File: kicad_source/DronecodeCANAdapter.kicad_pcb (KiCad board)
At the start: 2 copper layers, 65 x 30 mm, 31 parts, among them CN1 RASPI-IO, CN2 691322310004, CN3 GH_SM04B-GHS-TB, CN4 GH_SM04B-GHS-TB, SW1 JS202011JCQN, U1 MCP2518FD, U2 TCAN332GDR, Y1 RH100-20.000-20-3030-TR

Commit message: updated schematic and layout
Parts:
- removed C2, C3: 22pF, capacitors:C_0603
- removed C4: 100nF, capacitors:C_0603
- removed the D3 at (127.5, 94.5)
- removed L2: Label, labels:generationmake_logo
- removed R10, R11: 1k, resistors:R_0603
- removed R12: 2k, resistors:R_0603
- removed R5: 10k, resistors:R_0603
- removed R6, R7, R9: DNI, resistors:R_0603
- removed R8: 0R, resistors:R_0603
- removed SW1: JS202011JCQN, mechanical-switches:CK_JS202011JCQN
- removed U2: TCAN332GDR, SOIC:SOIJ-8_5.3x5.3mm_Pitch1.27mm
- removed Y1: RH100-20.000-20-3030-TR, crystals:Crystal_SMD_3.2x2.5mm_4Pad
- added D1: 150060GS75000, LEDs:LED_0603, F.Cu at (140.5, 98.0)
- added MECH1: MHP_3.2_5.0, MECH_mounting_holes:MHP_3.2_5.0, F.Cu at (140.5, 102.0)
- added MECH2: MHP_3.2_5.0, MECH_mounting_holes:MHP_3.2_5.0, F.Cu at (155.5, 102.0)
- CN1: value RASPI-IO -> CONN_01X05; footprint MODULE_compute:RASPI_ZERO_HAT_EDGE -> pin_headers:Pin_Header_Straight_1x05
- CN2: moved to B.Cu
- D2: value 150060GS75000 -> 150060RS75000
- L1: footprint labels:generationmake_small_solder -> labels:generationmake_small_silk; moved to B.Cu
- R1: value 0R -> 1k
- R2: value DNI -> 1k
- R3: value 10k -> 2k
- R4: value 120R -> DNI
- U1: value MCP2518FD -> TCAN332GDR; footprint SOIC:SOIC-14_3.9x8.7mm_Pitch1.27mm -> SOIC:SOIJ-8_5.3x5.3mm_Pitch1.27mm
- moved R4 27.4 mm to (144.0, 105.0), turned to 270 degrees
- moved C1 24.9 mm to (148.0, 96.5)
- moved CN2 24.5 mm to (148.0, 108.5), turned to 180 degrees
- moved D2 24.3 mm to (155.5, 98.0), turned to 180 degrees
- moved L1 22.7 mm to (148.0, 100.8), turned to 180 degrees
- moved R3 18.4 mm to (156.9, 109.0), turned to 90 degrees
- moved U1 10.4 mm to (148.0, 102.0), turned to 270 degrees
- moved D3 8.03 mm to (156.9, 106.2), turned to 270 degrees
- moved F1 7.68 mm to (141.4, 106.2), turned to 180 degrees
- moved CN1 4.61 mm to (143.0, 93.5), turned to 90 degrees
- moved R2 3.64 mm to (152.5, 98.0), turned to 0 degrees
- moved R1 2.69 mm to (143.5, 98.0), turned to 180 degrees
- moved D4 0.73 mm to (139.0, 109.0), turned to 270 degrees
- moved CN4 0.40 mm to (143.0, 113.3)
- renumbered D4 to D3, D1 to D4
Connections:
- CN1 pad 1: +3V3 -> +5V
- CN1 pad 2: +5V -> +3V3
- CN1 pad 3: (no net) -> /CAN_TX
- CN1 pad 4: +5V -> /CAN_RX
- CN1 pad 5: (no net) -> GND
- D3 pad 2: Net-(D4-Pad2) -> Net-(D3-Pad2)
- R1 pad 1: /SPI_CE0 -> /CAN_RX
- R1 pad 2: /MCP2517_CS -> Net-(D1-Pad2)
- R2 pad 1: /MCP2517_CS -> /CAN_TX
- R2 pad 2: /SPI_CE1 -> Net-(D2-Pad2)
- R3 pad 1: +3V3 -> /CANVCC
- R3 pad 2: /MCP2517_CS -> Net-(D3-Pad2)
- R4 pad 2: Net-(R4-Pad2) -> /CANH
- U1 pad 2: /CAN_RX -> GND
- U1 pad 3: (no net) -> +3V3
- U1 pad 4: /MCP2517_INT -> /CAN_RX
- U1 pad 5: /OSC2 -> (no net)
- U1 pad 6: /OSC1 -> /CANL
- U1 pad 7: GND -> /CANH
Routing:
- net GND: track 185.6 -> 60.4 mm, vias 22 -> 5
- net +3V3: track 70.5 -> 5.61 mm, vias 4 -> 0
- net /MCP2517_INT: track 30.1 -> 0.00 mm, vias 2 -> 0
- net /CANH: track 55.6 -> 26.8 mm
- net /INTERRUPT_24: track 23.1 -> 0.00 mm, vias 1 -> 0
- net /INTERRUPT_23: track 23.1 -> 0.00 mm, vias 1 -> 0
- net /CANVCC: track 43.9 -> 22.7 mm, vias 0 -> 3
- net /INTERRUPT_25: track 21.2 -> 0.00 mm, vias 1 -> 0
- net /SPI_CLK: track 20.5 -> 0.00 mm
- net +5V: track 36.2 -> 19.5 mm
- net /CANL: track 50.2 -> 35.1 mm
- net /SPI_MOSI: track 12.0 -> 0.00 mm
- net /SPI_MISO: track 11.5 -> 0.00 mm
- net /INTERRUPT_12: track 11.1 -> 0.00 mm
- net /MCP2517_CS: track 9.33 -> 0.00 mm
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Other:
- board size 65 x 30 mm -> 21 x 25 mm
- board text added: "3V3"
- board text added: "5V"
- board text added: "CAN RX"
- board text added: "CAN TX"
- board text added: "Dronecode CANAdapter 0.1"
- board text removed: "12"
- board text removed: "23"
- board text removed: "24"
- board text removed: "25"
- board text removed: "CANFDZeroHAT 0.2"
- board text removed: "CE0"
- board text removed: "CE1"
- board text removed: "VCC"
- board text removed: "chip select"
- board text removed: "for Microchip MCP2517FD or MCP2518FD"
- board text removed: "interrupt"
- board text removed: "termination on <-> off"

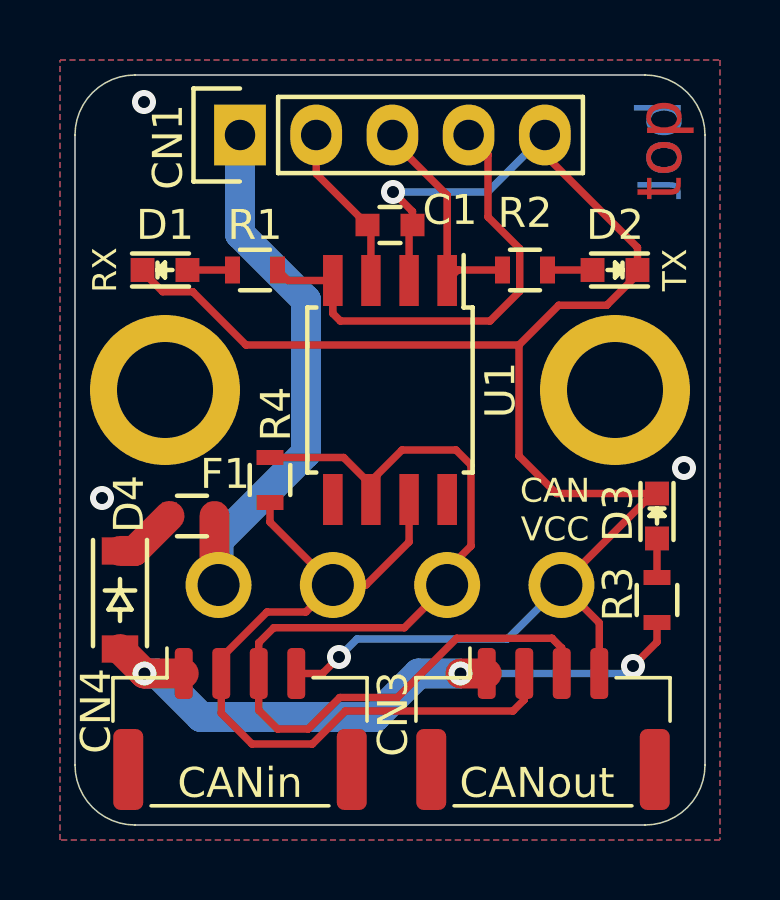
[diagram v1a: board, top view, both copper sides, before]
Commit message: corrected footprint of CAN transceiver
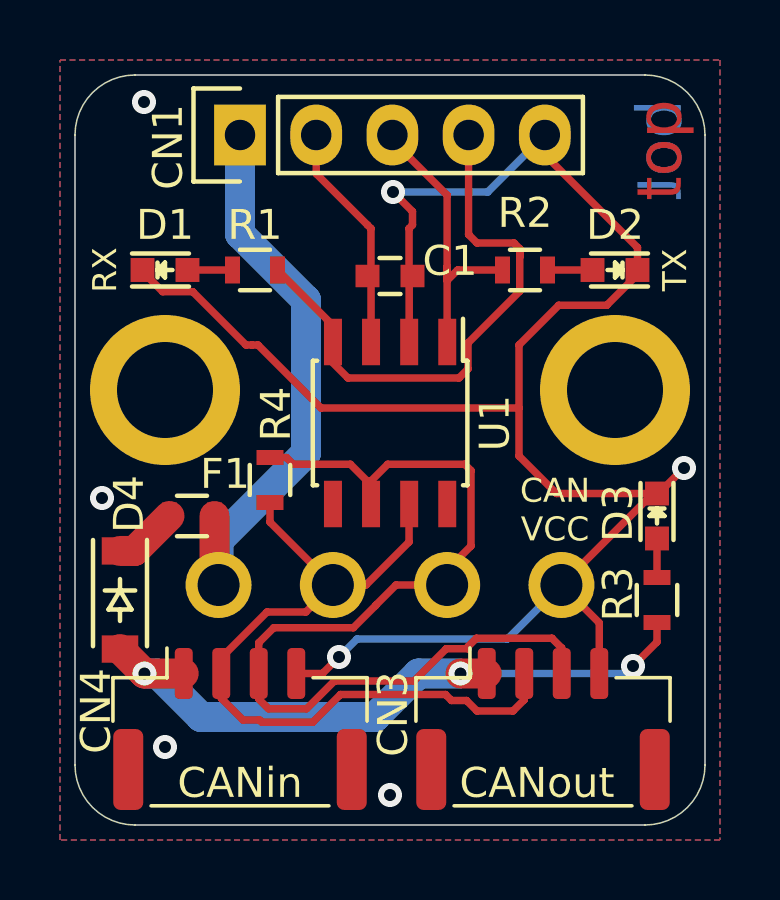
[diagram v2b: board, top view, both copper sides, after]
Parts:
- U1: footprint SOIC:SOIJ-8_5.3x5.3mm_Pitch1.27mm -> SOIC:SOIC-8_3.9x4.9mm_Pitch1.27mm
- moved C1 1.70 mm to (148.0, 98.2)
- moved U1 1.10 mm to (148.0, 103.1)
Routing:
- net GND: track 60.4 -> 64.7 mm, vias 5 -> 7
- net /CAN_TX: track 7.60 -> 10.1 mm
- net /CAN_RX: track 15.7 -> 18.2 mm
- net +3V3: track 5.61 -> 7.86 mm
- net /CANL: track 35.1 -> 33.8 mm
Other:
- board text added: "Dronecode CANAdapter 0.2"
- board text removed: "Dronecode CANAdapter 0.1"

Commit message: made debug leds low active
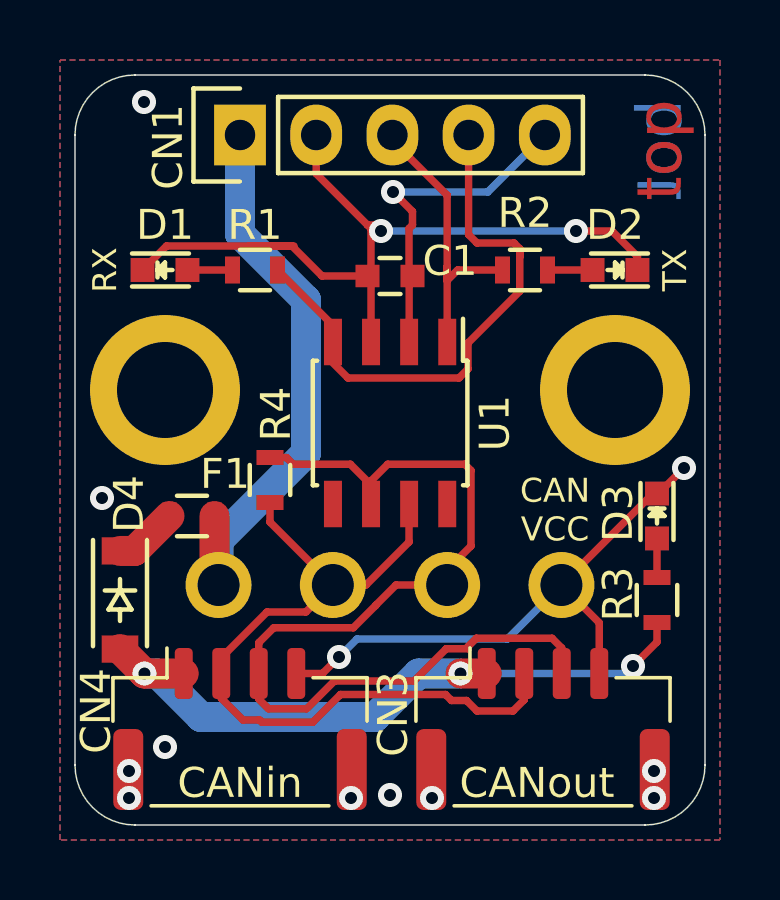
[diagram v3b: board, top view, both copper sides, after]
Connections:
- D1 pad 1: GND -> +3V3
- D2 pad 1: GND -> +3V3
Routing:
- net GND: track 64.7 -> 30.6 mm
- net +3V3: track 7.86 -> 27.5 mm, vias 0 -> 2
- net (no net): vias 0 -> 6

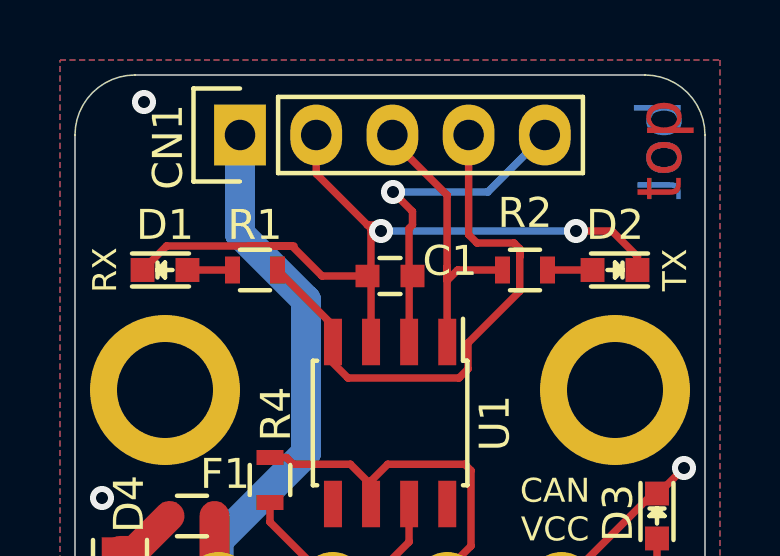
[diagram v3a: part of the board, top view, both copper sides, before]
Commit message: corrected polarity of leds
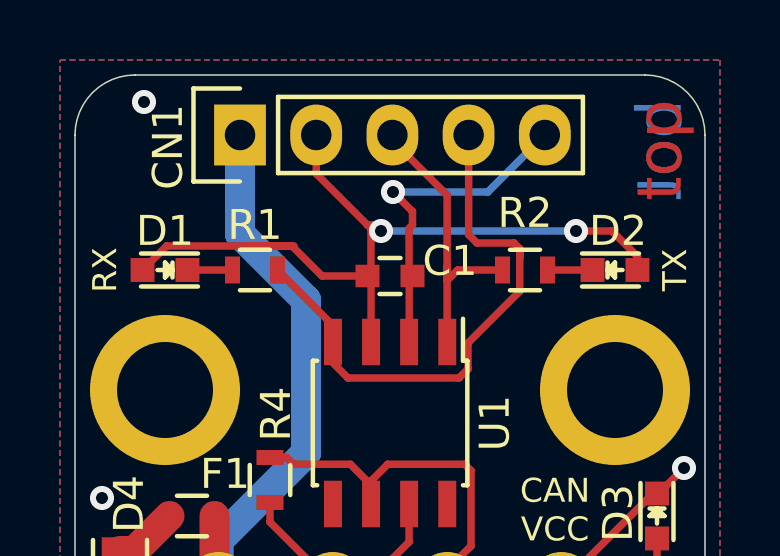
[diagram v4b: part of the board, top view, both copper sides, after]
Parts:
- turned D1 to 180 degrees
- turned D2 to 0 degrees
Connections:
- D1 pad 1: +3V3 -> Net-(D1-Pad1)
- D1 pad 2: Net-(D1-Pad2) -> +3V3
- D2 pad 1: +3V3 -> Net-(D2-Pad1)
- D2 pad 2: Net-(D2-Pad2) -> +3V3
- R1 pad 2: Net-(D1-Pad2) -> Net-(D1-Pad1)
- R2 pad 2: Net-(D2-Pad2) -> Net-(D2-Pad1)
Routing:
- net Net-(D2-Pad2): track 1.50 -> 0.00 mm
- net Net-(D2-Pad1): track 0.00 -> 1.50 mm
- net Net-(D1-Pad2): track 1.50 -> 0.00 mm
- net Net-(D1-Pad1): track 0.00 -> 1.50 mm
